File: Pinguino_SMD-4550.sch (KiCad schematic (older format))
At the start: 50 parts, among them P1 uUSB, P10 CONN_01X01, P11 CONN_01X01, P12 CONN_01X01, P13 CONN_01X01, P14 CONN_01X01, P15 CONN_01X01, P16 CONN_01X01, P17 CONN_01X01, P18 CONN_01X01, P19 CONN_01X01, P2 CONN_01X01, P20 CONN_01X01, P21 CONN_01X01, P22 CONN_01X01, P23 CONN_01X01, P24 CONN_01X01, P25 CONN_01X01, P26 CONN_01X01, P27 CONN_01X01, P28 CONN_01X01, P29 CONN_01X01, P3 CONN_01X01, P30 CONN_01X01, P31 CONN_01X01, P32 CONN_01X01, P33 CONN_01X01, P34 CONN_01X01, P35 CONN_01X01, P36 CONN_01X01, P37 CONN_01X01, P4 CONN_01X01, P5 CONN_01X01, P6 CONN_01X01, P7 CONN_01X01, P8 CONN_01X01, P9 CONN_01X01, SW1 Reset, U1 PIC18(L)F4550-I/PT, Y1 Crystal

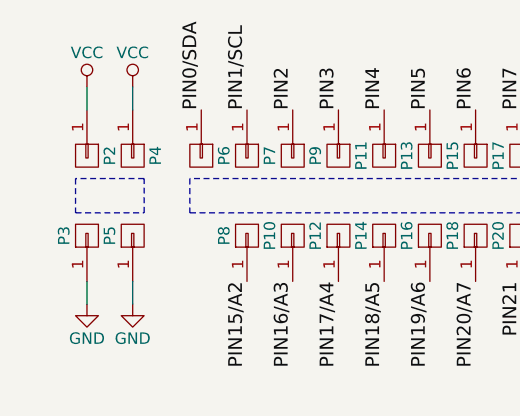
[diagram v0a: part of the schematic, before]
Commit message: Reorganized and aligned components. Capapol -> Tantalum B 3528.
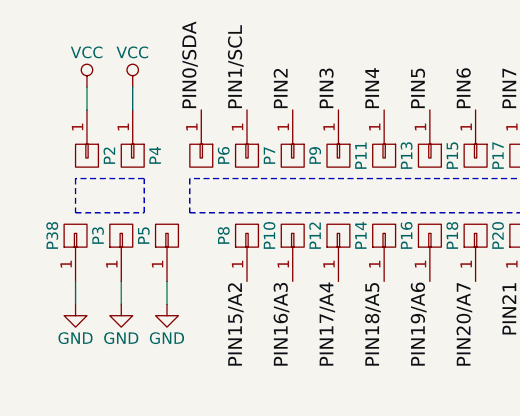
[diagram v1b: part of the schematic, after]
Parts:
- added P38: CONN_01X01, Socket_Strips:Socket_Strip_Straight_1x01, symbol CONN_01X01
- C5: footprint Capacitors_SMD:c_elec_6.3x5.3 -> Capacitors_Tantalum_SMD:TantalC_SizeB_EIA-3528_Wave
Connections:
- net GND: now also P38.1 (P1)
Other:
- moved on the sheet: P3, P5
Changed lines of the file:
@@
 F 0 "C5" H 9175 2000 50  0000 L CNN
 F 1 "10-100uF" V 9050 1750 50  0000 L CNN
-F 2 "Capacitors_SMD:c_elec_6.3x5.3" H 9188 1750 50  0001 C CNN
+F 2 "Capacitors_Tantalum_SMD:TantalC_SizeB_EIA-3528_Wave" H 9188 1750 50  0001 C CNN
 F 3 "" H 9150 1900 50  0000 C CNN
 	1    9150 1900
@@
 L GND #PWR020
 U 1 1 5849F351
-P 1350 6250
-F 0 "#PWR020" H 1350 6000 50  0001 C CNN
-F 1 "GND" H 1350 6100 50  0000 C CNN
-F 2 "" H 1350 6250 50  0000 C CNN
-F 3 "" H 1350 6250 50  0000 C CNN
-	1    1350 6250
+P 1500 6250
+F 0 "#PWR020" H 1500 6000 50  0001 C CNN
+F 1 "GND" H 1500 6100 50  0000 C CNN
+F 2 "" H 1500 6250 50  0000 C CNN
+F 3 "" H 1500 6250 50  0000 C CNN
+	1    1500 6250
 	1    0    0    -1
 $EndComp
@@
 L GND #PWR021
 U 1 1 5849F3C1
-P 1150 6250
-F 0 "#PWR021" H 1150 6000 50  0001 C CNN
-F 1 "GND" H 1150 6100 50  0000 C CNN
-F 2 "" H 1150 6250 50  0000 C CNN
-F 3 "" H 1150 6250 50  0000 C CNN
-	1    1150 6250
+P 1300 6250
+F 0 "#PWR021" H 1300 6000 50  0001 C CNN
+F 1 "GND" H 1300 6100 50  0000 C CNN
+F 2 "" H 1300 6250 50  0000 C CNN
+F 3 "" H 1300 6250 50  0000 C CNN
+	1    1300 6250
 	1    0    0    -1
 $EndComp
@@
 L CONN_01X01 P5
 U 1 1 5849FD31
-P 1350 5950
-F 0 "P5" H 1350 6050 50  0000 C CNN
-F 1 "CONN_01X01" V 1450 5950 50  0001 C CNN
-F 2 "Socket_Strips:Socket_Strip_Straight_1x01" H 1350 5950 50  0001 C CNN
-F 3 "" H 1350 5950 50  0000 C CNN
-	1    1350 5950
+P 1500 5950
+F 0 "P5" H 1500 6050 50  0000 C CNN
+F 1 "CONN_01X01" V 1600 5950 50  0001 C CNN
+F 2 "Socket_Strips:Socket_Strip_Straight_1x01" H 1500 5950 50  0001 C CNN
+F 3 "" H 1500 5950 50  0000 C CNN
+	1    1500 5950
 	0    -1   -1   0
 $EndComp
@@
 L CONN_01X01 P3
 U 1 1 5849FDE4
-P 1150 5950
-F 0 "P3" H 1150 6050 50  0000 C CNN
-F 1 "CONN_01X01" V 1250 5950 50  0001 C CNN
-F 2 "Socket_Strips:Socket_Strip_Straight_1x01" H 1150 5950 50  0001 C CNN
-F 3 "" H 1150 5950 50  0000 C CNN
-	1    1150 5950
-	0    -1   -1   0
-$EndComp
-Wire Wire Line
-	1150 6150 1150 6250
-Wire Wire Line
-	1350 6150 1350 6250
+P 1300 5950
+F 0 "P3" H 1300 6050 50  0000 C CNN
+F 1 "CONN_01X01" V 1400 5950 50  0001 C CNN
+F 2 "Socket_Strips:Socket_Strip_Straight_1x01" H 1300 5950 50  0001 C CNN
+F 3 "" H 1300 5950 50  0000 C CNN
+	1    1300 5950
+	0    -1   -1   0
+$EndComp
+Wire Wire Line
+	1300 6150 1300 6250
+Wire Wire Line
+	1500 6150 1500 6250
 Wire Notes Line
 	4500 5700 1600 5700
@@
 Text Label 5100 6000 0    60   ~ 0
 ICSP_PGC
+$Comp
+L CONN_01X01 P38
+U 1 1 5863069D
+P 1100 5950
+F 0 "P38" H 1100 6050 50  0000 C CNN
+F 1 "CONN_01X01" V 1200 5950 50  0001 C CNN
+F 2 "Socket_Strips:Socket_Strip_Straight_1x01" H 1100 5950 50  0001 C CNN
+F 3 "" H 1100 5950 50  0000 C CNN
+	1    1100 5950
+	0    -1   -1   0
+$EndComp
+$Comp
+L GND #PWR022
+U 1 1 58630752
+P 1100 6250
+F 0 "#PWR022" H 1100 6000 50  0001 C CNN
+F 1 "GND" H 1100 6100 50  0000 C CNN
+F 2 "" H 1100 6250 50  0000 C CNN
+F 3 "" H 1100 6250 50  0000 C CNN
+	1    1100 6250
+	1    0    0    -1
+$EndComp
+Wire Wire Line
+	1100 6150 1100 6250
 $EndSCHEMATC
